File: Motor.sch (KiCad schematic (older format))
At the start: 1 part

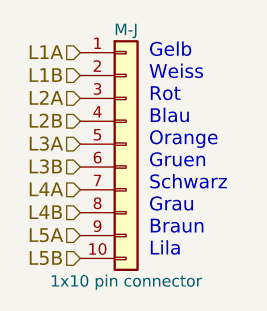
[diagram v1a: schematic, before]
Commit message: Added and connected sixth L298N symbol
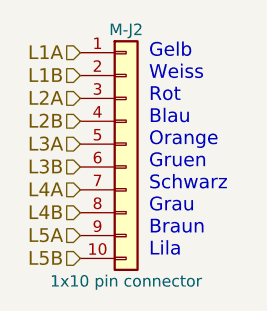
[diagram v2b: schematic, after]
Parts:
- renumbered M-J to M-J1
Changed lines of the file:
@@
 $Descr A4 11693 8268
 encoding utf-8
-Sheet 3 10
+Sheet 3 11
 Title ""
 Date ""
@@
 $EndDescr
 $Comp
-L Conn_01x10 M-J
+L Conn_01x10 M-J1
 U 1 1 5A2524C5
 P 4850 3900
-F 0 "M-J" H 4850 4400 50  0000 C CNN
+AR Path="/5A24BC5B/5A2524C5" Ref="M-J1"  Part="1"
+AR Path="/5A257129/5A2524C5" Ref="M-J2"  Part="1"
+F 0 "M-J2" H 4850 4400 50  0000 C CNN
 F 1 "1x10 pin connector" H 4850 3300 50  0000 C CNN
 F 2 "" H 4850 3900 50  0001 C CNN
